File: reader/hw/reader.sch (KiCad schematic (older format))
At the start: 37 parts, among them P101 Wago_233-502, P102 Wago_233-502, P103 CONN_02X05, P104 JST, P105 CONN_01X08, Q101 MMBT2222A, Q102 MMBT2222A, U101 LP2992AIM5-3.3CT-ND, U102 SN75176BDR, U103 MKE04P24M48SF0, X101 CRYSTAL

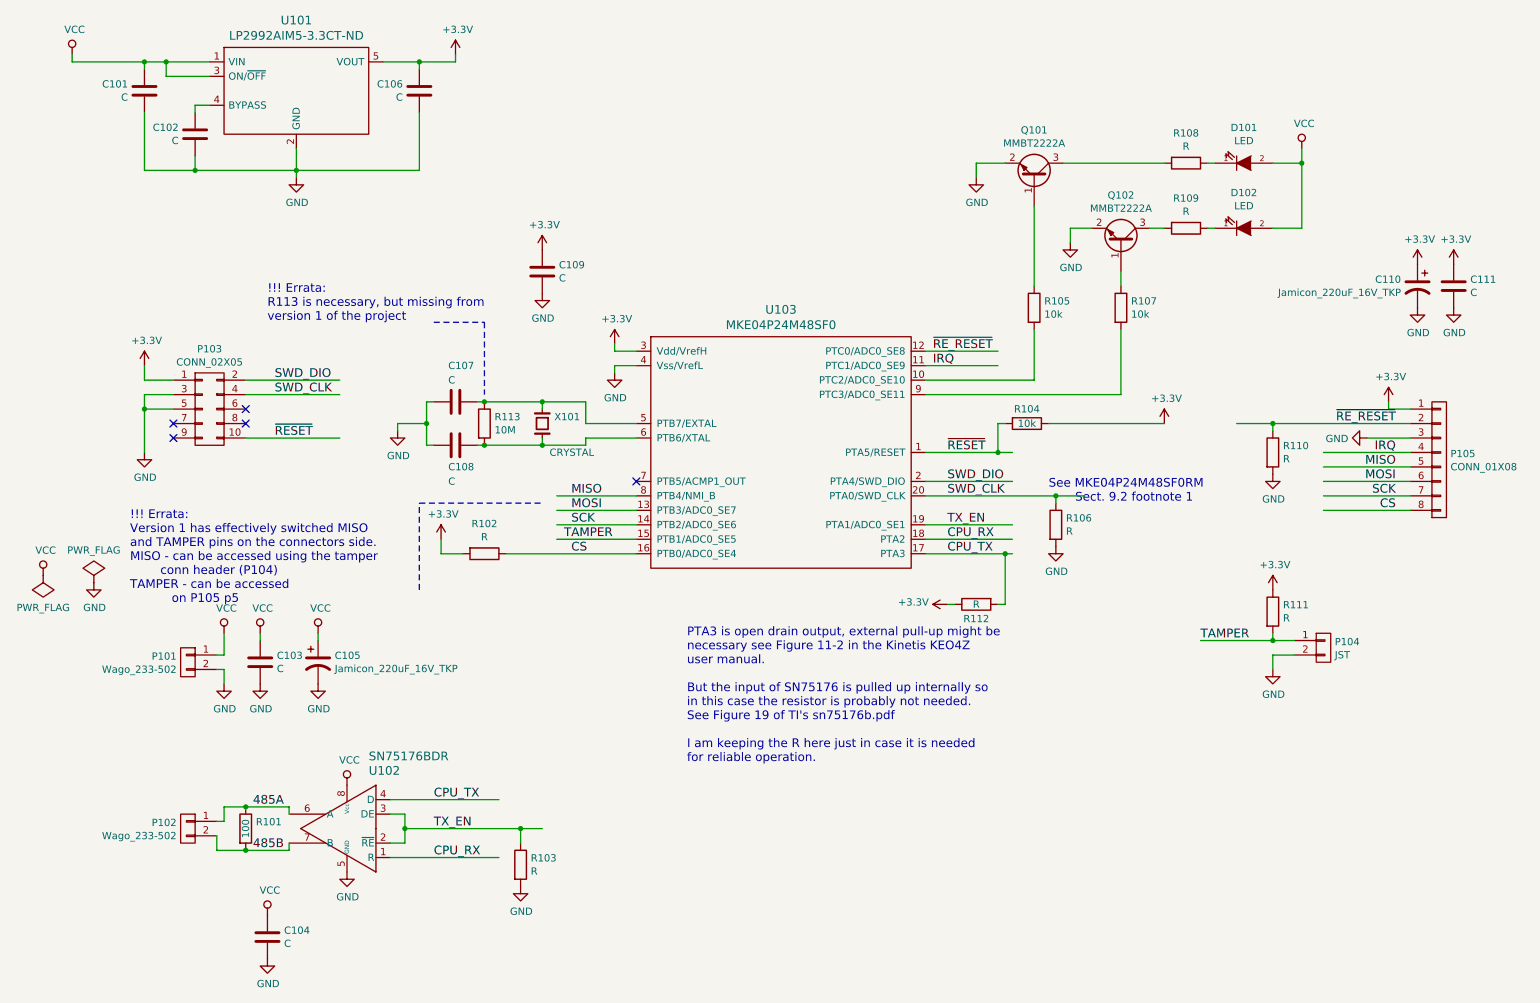
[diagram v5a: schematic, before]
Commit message: schematic improvements (door state pin for controller, fixes)
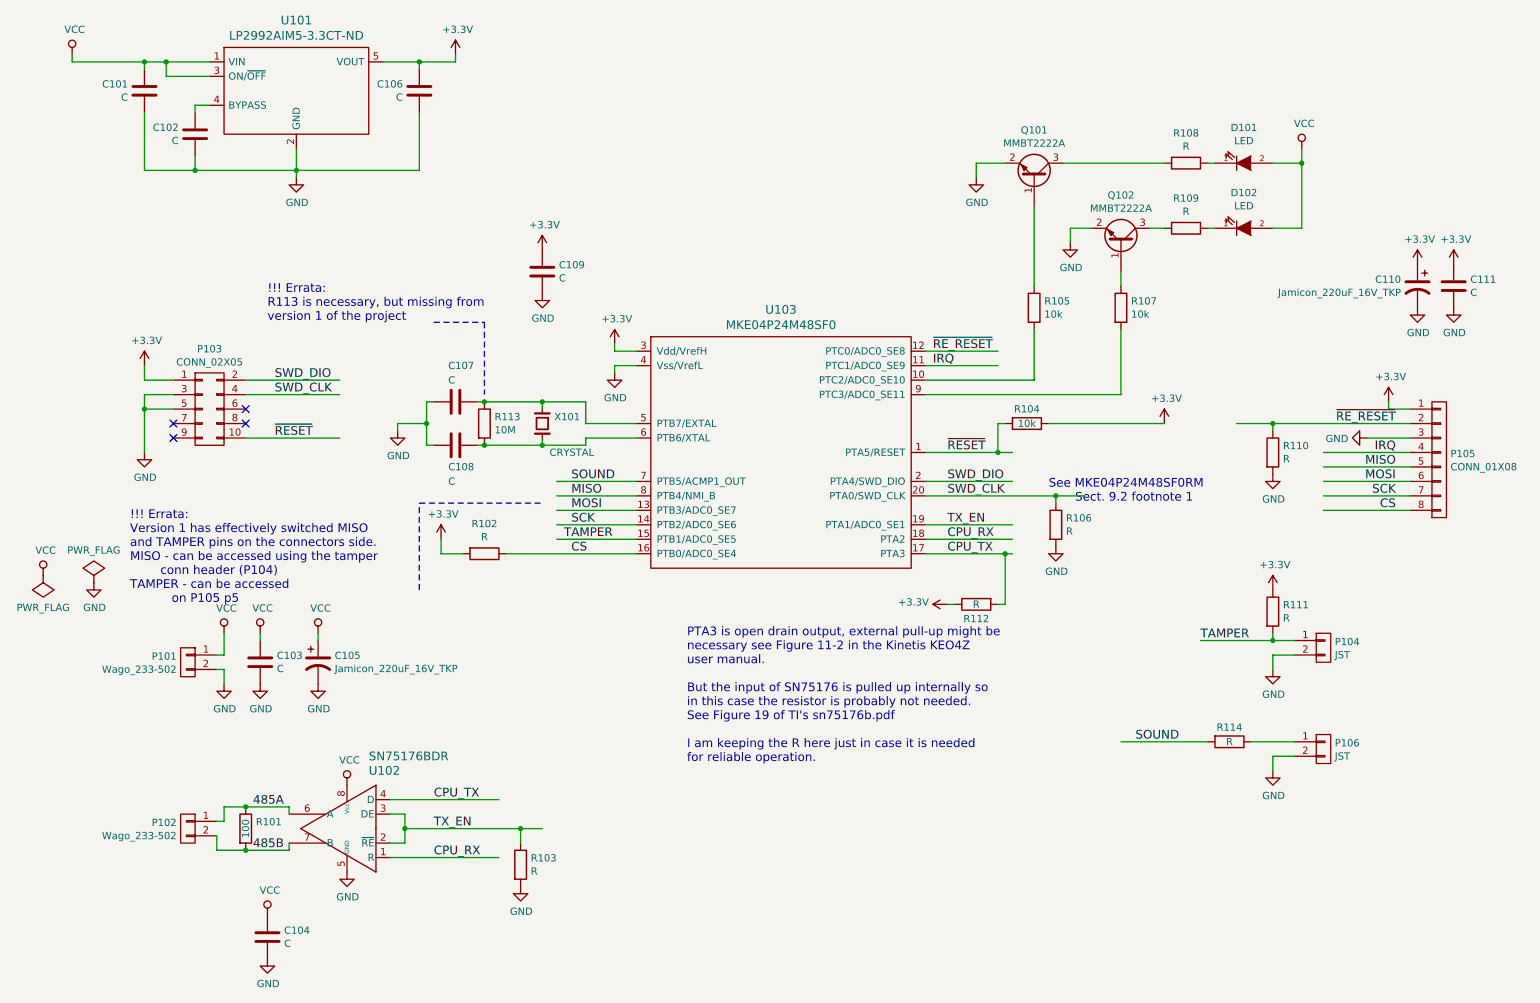
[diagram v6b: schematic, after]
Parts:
- added P106: JST, th-normal:Connector_JST_PHR-2, symbol connectors:CONN_01X02
- added R114: R, symbol simple:R
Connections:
- net labels added: SOUND
- wire segments 113 -> 140
- no-connect marks 5 -> 4
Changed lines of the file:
@@
 	2000 6500 2000 6400
 Wire Wire Line
-	2000 6400 2450 6400
+	2000 6400 2150 6400
 Wire Wire Line
 	2450 6400 2450 6450
@@
 	1950 6600 1950 6700
 Wire Wire Line
-	1950 6700 2450 6700
+	1950 6700 2150 6700
 Wire Wire Line
 	2450 6700 2450 6650
@@
 SCK
 Wire Wire Line
-	6850 4650 7450 4650
+	6850 4650 7400 4650
 Wire Wire Line
 	4850 4350 4300 4350
@@
 	1650 3550 1450 3550
 Wire Wire Line
-	1450 3550 1450 3950
+	1450 3550 1450 3650
 Wire Wire Line
 	1650 3650 1450 3650
@@
 	2150 3850 2800 3850
 Wire Wire Line
-	6850 3950 7450 3950
+	6850 3950 7350 3950
 Wire Wire Line
 	6850 4150 7450 4150
 Wire Wire Line
-	6850 4250 7950 4250
+	6850 4250 7750 4250
 $Comp
 L mspower:VCC #PWR09
@@
 	1450 1250 1450 1300
 Wire Wire Line
-	950  1250 1900 1250
+	950  1250 1450 1250
 Connection ~ 1450 1250
 Wire Wire Line
@@
 	1450 1600 1450 2000
 Wire Wire Line
-	1450 2000 3350 2000
+	1450 2000 1800 2000
 Wire Wire Line
 	1800 1900 1800 2000
 Connection ~ 1800 2000
 Wire Wire Line
-	2500 1850 2500 2050
+	2500 1850 2500 2000
 Wire Wire Line
 	3350 2000 3350 1600
 Wire Wire Line
-	3100 1250 3600 1250
+	3100 1250 3350 1250
 Wire Wire Line
 	3350 1250 3350 1300
@@
 	3150 6450 3250 6450
 Wire Wire Line
-	3250 6450 3250 6650
-Wire Wire Line
-	3250 6550 4200 6550
+	3250 6450 3250 6550
+Wire Wire Line
+	3250 6550 4050 6550
 Wire Wire Line
 	3250 6650 3150 6650
@@
 	9250 1950 9450 1950
 Wire Wire Line
-	9450 1850 9450 2400
+	9450 1850 9450 1950
 Wire Wire Line
 	9450 2400 9250 2400
@@
 $EndComp
 Wire Wire Line
-	8750 5250 9400 5250
+	8750 5250 9250 5250
 Wire Wire Line
 	9250 5200 9250 5250
@@
 	3200 3750 3400 3750
 Wire Wire Line
-	3400 3600 3400 3900
+	3400 3600 3400 3750
 Wire Wire Line
 	3400 3600 3450 3600
@@
 $EndComp
 Wire Wire Line
-	3750 3600 4500 3600
+	3750 3600 3800 3600
 Wire Wire Line
 	4200 3600 4200 3650
 Wire Wire Line
-	3750 3900 4500 3900
+	3750 3900 3800 3900
 Wire Wire Line
 	4200 3900 4200 3850
@@
 	10050 3650 10200 3650
 Wire Wire Line
-	9000 3750 10200 3750
+	9000 3750 9250 3750
 Wire Wire Line
 	10200 3850 9900 3850
@@
 	1    0    0    -1
 $EndComp
-NoConn ~ 4850 4150
 Connection ~ 2500 2000
 Text Label 2200 6400 0    60   ~ 0
@@
 Wire Notes Line
 	3800 3050 3800 3550
+Wire Wire Line
+	2150 6400 2450 6400
+Wire Wire Line
+	2150 6700 2450 6700
+Wire Wire Line
+	1450 3650 1450 3950
+Wire Wire Line
+	1450 1250 1600 1250
+Wire Wire Line
+	1600 1250 1900 1250
+Wire Wire Line
+	1800 2000 2500 2000
+Wire Wire Line
+	3350 1250 3600 1250
+Wire Wire Line
+	7350 3950 7450 3950
+Wire Wire Line
+	3250 6550 3250 6650
+Wire Wire Line
+	4050 6550 4200 6550
+Wire Wire Line
+	9450 1950 9450 2400
+Wire Wire Line
+	9250 5250 9400 5250
+Wire Wire Line
+	7750 4250 7950 4250
+Wire Wire Line
+	3400 3750 3400 3900
+Wire Wire Line
+	4200 3900 4500 3900
+Wire Wire Line
+	4200 3600 4500 3600
+Wire Wire Line
+	9250 3750 10200 3750
+Wire Wire Line
+	2500 2000 2500 2050
+Wire Wire Line
+	2500 2000 3350 2000
+Wire Wire Line
+	7400 4650 7450 4650
+Wire Wire Line
+	3800 3600 4200 3600
+Wire Wire Line
+	3800 3900 4200 3900
+Wire Wire Line
+	4850 4150 4300 4150
+Text Label 4400 4150 0    60   ~ 0
+SOUND
+$Comp
+L connectors:CONN_01X02 P106
+U 1 1 5A32303C
+P 9600 6000
+F 0 "P106" H 9678 6041 50  0000 L CNN
+F 1 "JST" H 9678 5950 50  0000 L CNN
+F 2 "th-normal:Connector_JST_PHR-2" H 9600 6000 60  0001 C CNN
+F 3 "" H 9600 6000 60  0000 C CNN
+	1    9600 6000
+	1    0    0    -1
+$EndComp
+$Comp
+L mspower:GND #PWR037
+U 1 1 5A323042
+P 9250 6150
+F 0 "#PWR037" H 9250 5900 50  0001 C CNN
+F 1 "GND" H 9255 5977 50  0000 C CNN
+F 2 "" H 9250 6150 60  0000 C CNN
+F 3 "" H 9250 6150 60  0000 C CNN
+	1    9250 6150
+	1    0    0    -1
+$EndComp
+Wire Wire Line
+	9400 6050 9250 6050
+Wire Wire Line
+	9250 6050 9250 6150
+Text Label 8300 5950 0    60   ~ 0
+SOUND
+$Comp
+L simple:R R114
+U 1 1 5A32D8F3
+P 8950 5950
+F 0 "R114" V 8850 5950 50  0000 C CNN
+F 1 "R" V 8950 5950 50  0000 C CNN
+F 2 "" V 8880 5950 30  0000 C CNN
+F 3 "" H 8950 5950 30  0000 C CNN
+	1    8950 5950
+	0    1    1    0
+$EndComp
+Wire Wire Line
+	9100 5950 9400 5950
+Wire Wire Line
+	8200 5950 8800 5950
 $EndSCHEMATC
